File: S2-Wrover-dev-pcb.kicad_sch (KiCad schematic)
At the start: 24 parts, among them J1 USB_C_Receptacle_USB2.0, J2 Jack-DC, P1 CONN_02X13, P3 CONN_02X13, SW1 RESET, SW2 BOOT, U1 MCP1700-1202E_SOT23, U2 ESP32-S2-WROVER, U3 TPS2113APW, U4 TP4056

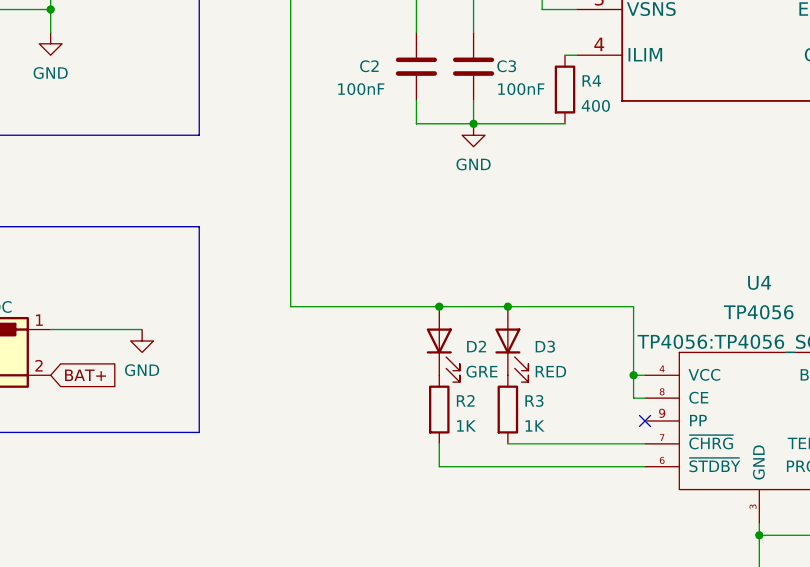
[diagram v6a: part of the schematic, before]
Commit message: Add Schottky btw. VBUS & TP4056 VCC
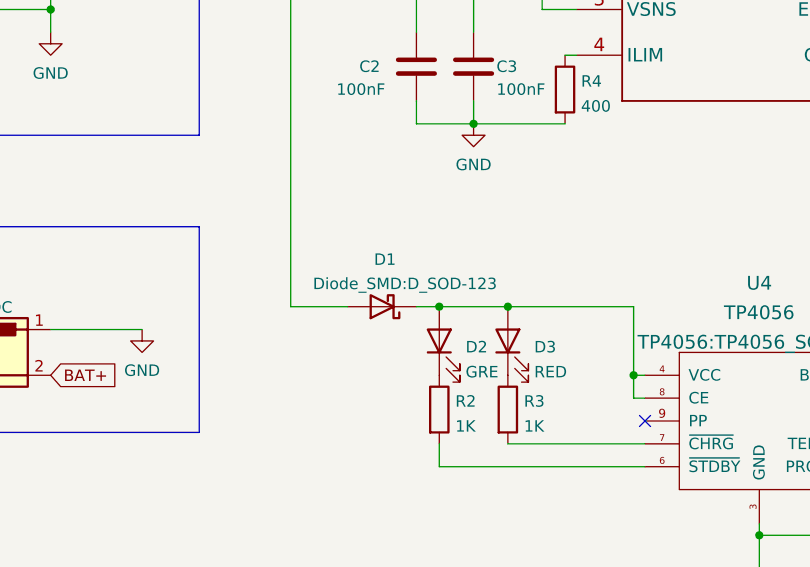
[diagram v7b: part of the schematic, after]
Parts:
- added D1: D_Schottky, Diode_SMD:D_SOD-123, symbol Device:D_Schottky
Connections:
- net VBUS: now also D1.2 (A); no longer D2.2 (A), D3.2 (A), U4.4 (VCC), U4.8 (CE)
- new net: D1.1 (K), D2.2 (A), D3.2 (A), U4.4 (VCC), U4.8 (CE)
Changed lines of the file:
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@@
   (junction (at 264.16 111.76) (diameter 0) (color 0 0 0 0)
   )
+  (junction (at 215.9 86.36) (diameter 0) (color 0 0 0 0)
+  )
   (junction (at 140.97 92.71) (diameter 0) (color 0 0 0 0)
   )
@@
   )
   (junction (at 171.45 161.29) (diameter 0) (color 0 0 0 0)
-  )
-  (junction (at 215.9 86.36) (diameter 0) (color 0 0 0 0)
   )
   (junction (at 219.71 66.04) (diameter 0) (color 0 0 0 0)
@@
     (stroke (width 0) (type default) (color 0 0 0 0))
   )
+  (wire (pts (xy 199.39 86.36) (xy 205.74 86.36))
+    (stroke (width 0) (type default) (color 0 0 0 0))
+  )
   (wire (pts (xy 171.45 135.89) (xy 171.45 138.43))
     (stroke (width 0) (type default) (color 0 0 0 0))
@@
     (stroke (width 0) (type default) (color 0 0 0 0))
   )
+  (wire (pts (xy 213.36 86.36) (xy 215.9 86.36))
+    (stroke (width 0) (type default) (color 0 0 0 0))
+  )
   (wire (pts (xy 266.7 58.42) (xy 273.05 58.42))
     (stroke (width 0) (type default) (color 0 0 0 0))
@@
   )
   (polyline (pts (xy 189.23 26.67) (xy 138.43 26.67))
-    (stroke (width 0) (type default) (color 0 0 0 0))
-  )
-  (wire (pts (xy 199.39 86.36) (xy 215.9 86.36))
     (stroke (width 0) (type default) (color 0 0 0 0))
   )
@@
     (pin "1")
   )
+  (symbol (lib_id "Device:D_Schottky") (at 209.55 86.36 180) (unit 1)
+    (in_bom yes) (on_board yes)
+    (property "Reference" "D1" (id 0) (at 209.8675 81.1235 0))
+    (property "Value" "D_Schottky" (id 1) (at 209.8675 83.8986 0)
+      (effects (font (size 1.27 1.27)) hide)
+    )
+    (property "Footprint" "Diode_SMD:D_SOD-123" (id 2) (at 212.09 83.82 0))
+    (property "Datasheet" "http://www.vishay.com/docs/88525/1n5817.pdf" (id 3) (at 209.55 86.36 0)
+      (effects (font (size 1.27 1.27)) hide)
+    )
+    (property "LCSC" "C8598" (id 4) (at 209.55 86.36 0)
+      (effects (font (size 1.27 1.27)) hide)
+    )
+    (pin "1")
+    (pin "2")
+  )
   (symbol (lib_id "power:GND") (at 219.71 66.04 0) (unit 1)
     (in_bom yes) (on_board yes) (fields_autoplaced)
@@
       (reference "C5") (unit 1) (value "0.1u") (footprint "Capacitor_SMD:C_0805_2012Metric")
     )
+    (path "/77f65cef-2bce-414e-8b99-31f9cd0b59b0"
+      (reference "D1") (unit 1) (value "D_Schottky") (footprint "Diode_SMD:D_SOD-123")
+    )
     (path "/e0ce6cb3-5c01-43ad-bab7-b796f3a1bb0f"
